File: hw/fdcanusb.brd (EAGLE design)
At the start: 41 x 32 mm, 37 parts, among them J1 MF-CON-MICROUSB-RIGHT, J3 JST-ZH6SMT_VERT, M1 MOUNT, M2 MOUNT, M3 MOUNT, M4 MOUNT, U1 MF-REG-SOT235-3.3V-300mA, U2 USBLC6-2SC6, U3 TCAN334GSOT23, U4 TLP3317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

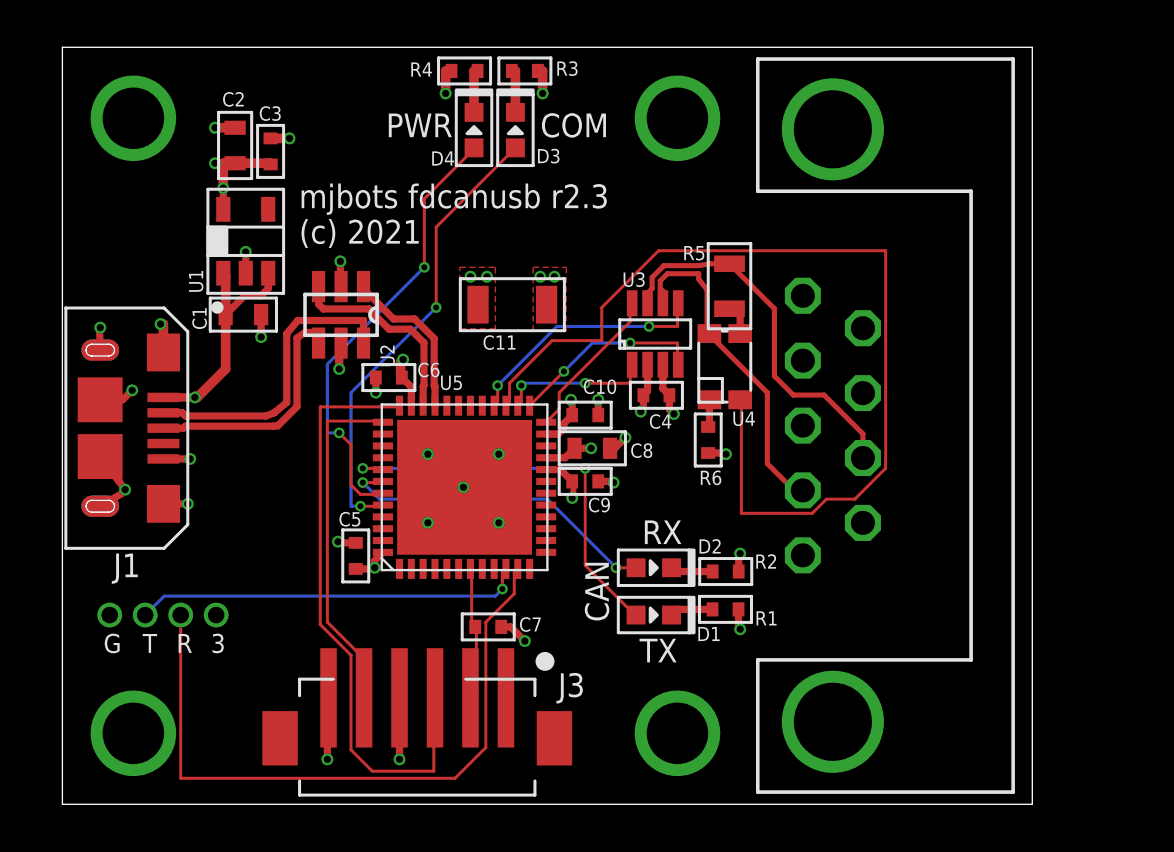
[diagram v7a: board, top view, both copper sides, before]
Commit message: Delete some wire stubs and approve more dimension DRCs
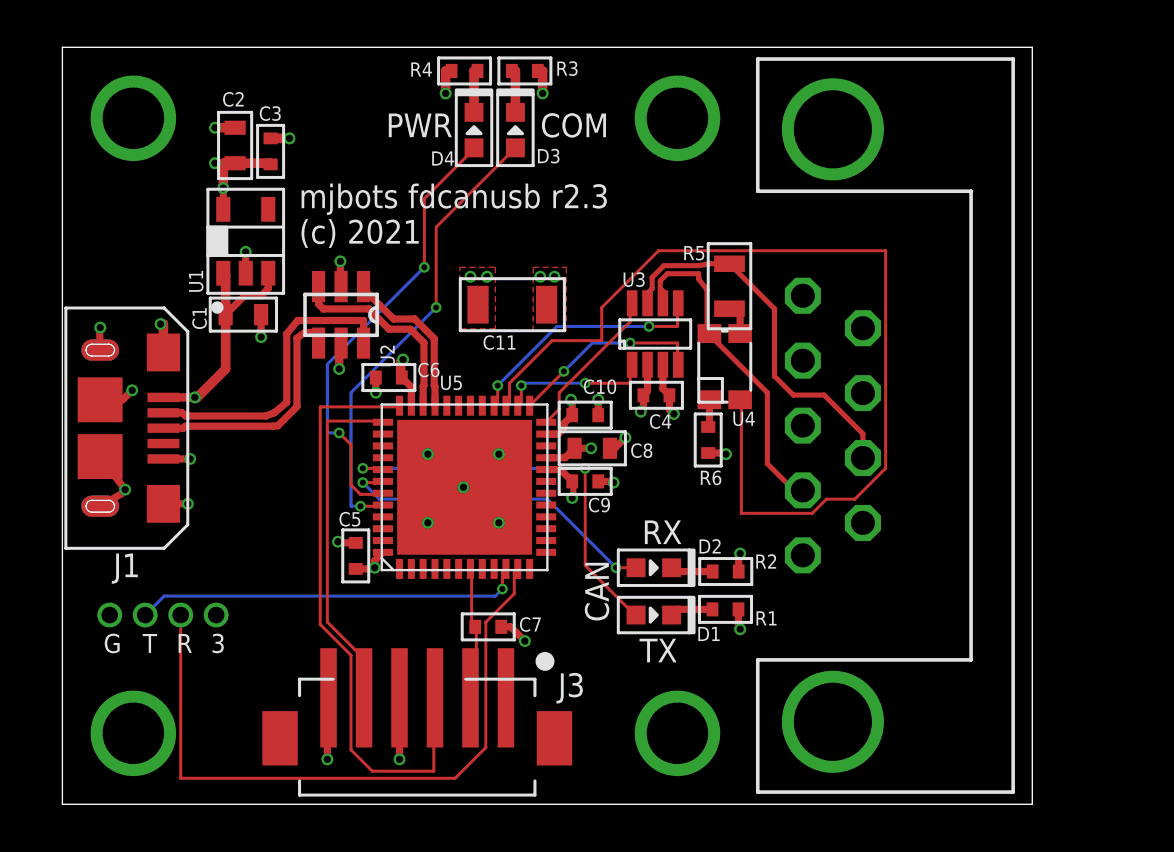
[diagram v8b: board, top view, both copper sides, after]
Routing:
- net GND: track 30.9 -> 27.2 mm
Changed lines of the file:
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@@
 <wire x1="20.1" y1="31" x2="20.3" y2="31" width="0.4064" layer="1"/>
 <wire x1="20.3" y1="31" x2="20.3" y2="30.05" width="0.4064" layer="1"/>
-<wire x1="12.5" y1="11.15" x2="12.4" y2="11.05" width="0.3048" layer="1"/>
 <wire x1="12.4" y1="11.05" x2="11.7" y2="11.05" width="0.3048" layer="1"/>
 <wire x1="11.7" y1="11.05" x2="11.65" y2="11.1" width="0.3048" layer="1"/>
@@
 <wire x1="22.65" y1="13.65" x2="23.25" y2="13.65" width="0.3048" layer="1"/>
 <wire x1="23.25" y1="13.65" x2="23.3" y2="13.6" width="0.3048" layer="1"/>
-<wire x1="17.25" y1="13.65" x2="17" y2="13.4" width="0.3048" layer="1"/>
 <wire x1="24.735" y1="18.58" x2="24.735" y2="17.465" width="0.3048" layer="1"/>
 <wire x1="24.735" y1="17.465" x2="24.56" y2="17.29" width="0.3048" layer="1"/>
@@
 <wire x1="11.78" y1="21.8838" x2="11.75" y2="21.9138" width="0.3048" layer="1"/>
 <wire x1="11.75" y1="21.9138" x2="11.75" y2="22.95" width="0.3048" layer="1"/>
-<wire x1="19.25" y1="15.65" x2="17" y2="13.4" width="0.254" layer="1" curve="90"/>
 <wire x1="17" y1="13.4" x2="16.95" y2="13.4" width="0.127" layer="1"/>
 <contactref element="J1" pad="S5"/>
@@
 <wire x1="6.8" y1="25.15" x2="6.8" y2="26" width="0.3048" layer="1"/>
 <wire x1="6.8" y1="26" x2="6.8" y2="26.05" width="0.3048" layer="1"/>
-<wire x1="7.3" y1="27.05" x2="7.3" y2="27.1" width="0.3048" layer="1"/>
 <via x="6.45" y="27.1" extent="1-16" drill="0.3048"/>
 <wire x1="7.3" y1="27.1" x2="6.45" y2="27.1" width="0.3048" layer="1"/>
@@
 <contactref element="C7" pad="P$1"/>
 <contactref element="J3" pad="2"/>
-<wire x1="17.25" y1="4.5" x2="17.45" y2="4.7" width="0.3048" layer="1"/>
 <wire x1="17.3" y1="7.6" x2="17.4" y2="7.5" width="0.127" layer="1"/>
 <wire x1="17.3" y1="9.9" x2="17.3" y2="7.6" width="0.127" layer="1"/>
